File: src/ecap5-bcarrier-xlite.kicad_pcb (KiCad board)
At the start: 2 copper layers, 160 x 60 mm, 48 parts, among them J1 DDR4_SODIMM_Board, J2 DDR4_SODIMM_Board, J3 Conn_02x04_Counter_Clockwise, J5 USB_C_Receptacle_USB2.0_14P, J6 Conn_Coaxial, J7 Conn_Coaxial, J8 Conn_Coaxial, J9 1935161, Q1 BC846BR13, Q2 BC846BR13, SW1 RESET_SOM1, SW2 RESET_SOM2, SW3 USER1, SW4 USER1, U1 FT232RN, U2 AP7375-33SA-7

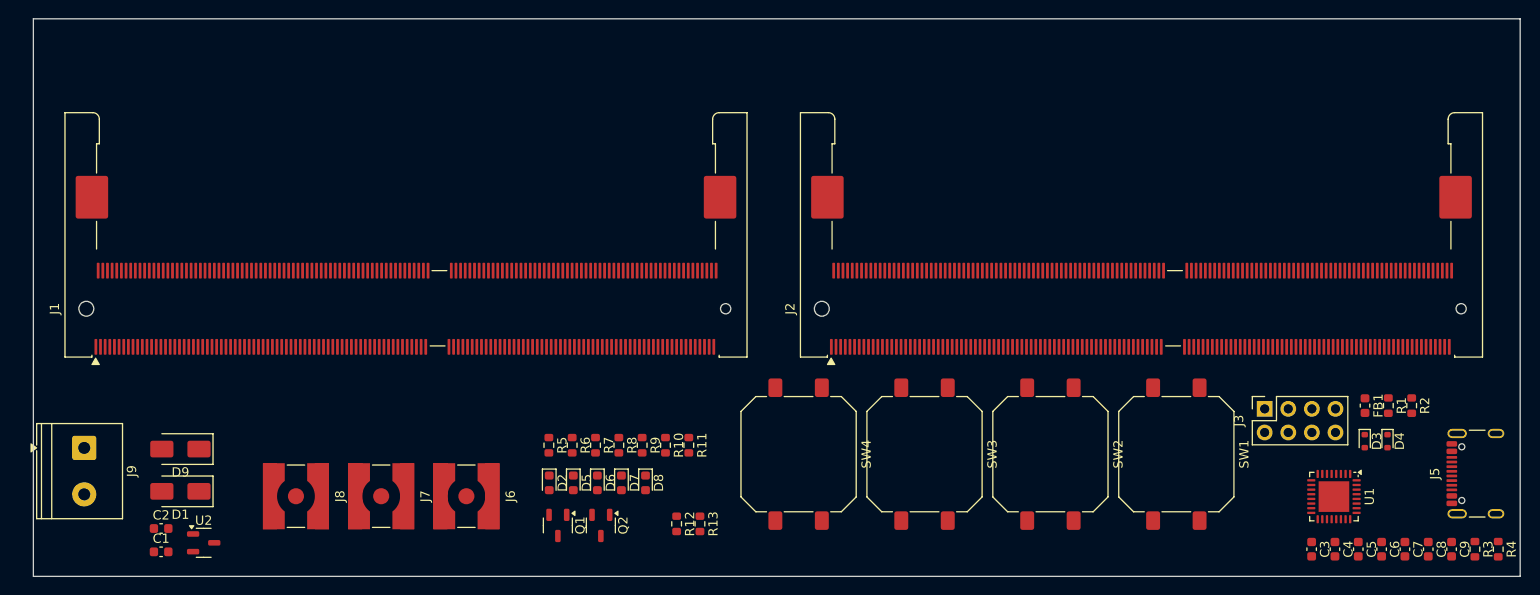
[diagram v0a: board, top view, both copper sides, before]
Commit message: Add power planes
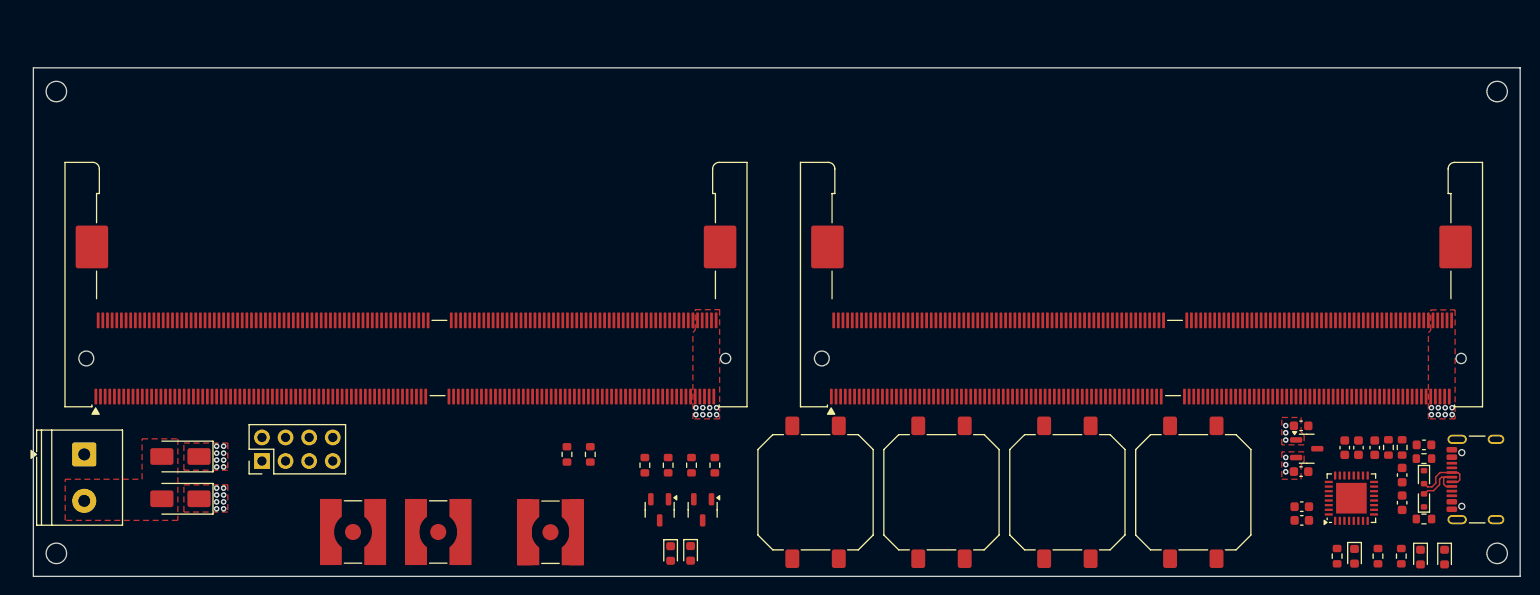
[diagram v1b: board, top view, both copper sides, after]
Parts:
- added H1: MountingHole, MountingHole:MountingHole_2.2mm_M2, F.Cu at (34.7, 66.0)
- added H2: MountingHole, MountingHole:MountingHole_2.2mm_M2, F.Cu at (189.8, 66.0)
- added H3: MountingHole, MountingHole:MountingHole_2.2mm_M2, F.Cu at (189.8, 115.7)
- added H4: MountingHole, MountingHole:MountingHole_2.2mm_M2, F.Cu at (34.7, 115.7)
- J3: footprint Connector_PinSocket_2.54mm:PinSocket_2x04_P2.54mm_Vertical -> Connector_PinHeader_2.54mm:PinHeader_2x04_P2.54mm_Vertical
- moved C1 123.4 mm to (168.7, 102.0)
- moved C2 122.8 mm to (168.7, 106.9)
- moved U2 119.1 mm to (169.3, 104.5)
- moved J3 108.1 mm to (56.9, 105.8)
- moved D6 88.9 mm to (181.5, 116.1)
- moved D7 88.9 mm to (184.1, 116.1)
- moved R7 87.5 mm to (179.5, 116.0)
- moved R6 87.5 mm to (176.9, 116.0)
- moved R5 85.7 mm to (172.6, 116.0)
- moved D5 84.4 mm to (174.4, 116.0)
- moved R4 16.1 mm to (178.1, 104.3), turned to 90 degrees
- moved D2 15.1 mm to (100.8, 115.7)
- moved R12 14.0 mm to (89.7, 105.1)
- moved R13 14.0 mm to (92.2, 105.1)
- moved C9 13.7 mm to (176.6, 104.3), turned to 90 degrees
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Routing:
- net /USB.DP: track 0.00 -> 6.65 mm
- net /USB.DN: track 0.00 -> 6.64 mm
- net VIN9_15: vias 0 -> 27
- net GND: vias 0 -> 8
- net +3V3: vias 0 -> 3
- added copper zone on F.Cu, net +3V3
- added copper zone on In2.Cu, net +3V3
- added copper zone on F.Cu, net GND
- added copper zone on In1.Cu, net GND
- added copper zone on F.Cu, net Net-(D1-A)
- added copper zone on F.Cu, net VIN9_15
- added copper zone on In2.Cu, net VIN9_15
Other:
- board size 160 x 60 mm -> 160 x 54.7 mm
- copper layers 2 -> 4

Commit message: Start routing the usb interface
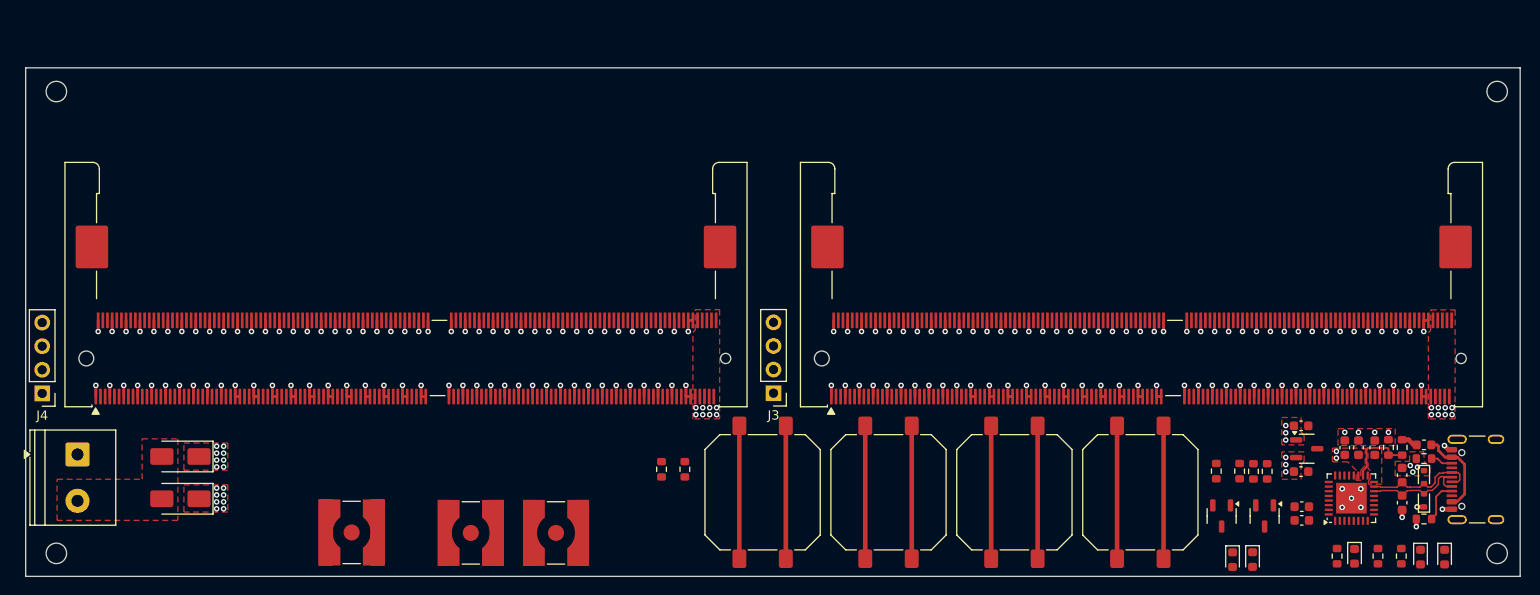
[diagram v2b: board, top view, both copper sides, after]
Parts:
- added J4: Conn_01x04, Connector_PinHeader_2.54mm:PinHeader_1x04_P2.54mm_Vertical, F.Cu at (33.2, 98.5)
- J3: value Conn_02x04_Counter_Clockwise -> Conn_01x04; footprint Connector_PinHeader_2.54mm:PinHeader_2x04_P2.54mm_Vertical -> Connector_PinHeader_2.54mm:PinHeader_1x04_P2.54mm_Vertical
- moved R8 61.5 mm to (159.6, 106.9)
- moved R9 61.5 mm to (162.1, 106.9)
- moved D2 60.5 mm to (161.3, 116.4)
- moved R10 60.5 mm to (163.6, 106.9)
- moved D8 60.5 mm to (163.4, 116.4)
- moved Q1 60.5 mm to (160.1, 111.7)
- moved Q2 60.5 mm to (164.8, 111.7)
- moved R11 59.4 mm to (165.0, 106.9)
- moved J3 55.5 mm to (111.9, 98.5), turned to 180 degrees
- moved J6 21.4 mm to (66.5, 113.5)
- moved J7 12.7 mm to (88.5, 113.5)
- moved J8 12.7 mm to (79.3, 113.5)
- moved R12 10.3 mm to (99.8, 106.7)
- moved R13 10.3 mm to (102.4, 106.7)
- moved R1 6.50 mm to (181.9, 112.0)
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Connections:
- J1 pad 11: /SOM1/JTAG_TDO -> /SOM1.JTAC_TDO
- J1 pad 3: /SOM1/JTAG_TMS -> /SOM1.JTAC_TMS
- J1 pad 5: /SOM1/JTAG_TCK -> /SOM1.JTAC_TCK
- J1 pad 9: /SOM1/JTAG_TDI -> /SOM1.JTAC_TDI
- J2 pad 11: /SOM2/JTAG_TDO -> /SOM2.JTAC_TDO
- J2 pad 3: /SOM2/JTAG_TMS -> /SOM2.JTAC_TMS
- J2 pad 5: /SOM2/JTAG_TCK -> /SOM2.JTAC_TCK
- J2 pad 9: /SOM2/JTAG_TDI -> /SOM2.JTAC_TDI
- J3 pad 1: /SOM1.JTAC_TCK -> /SOM2.JTAC_TCK
- J3 pad 2: /SOM1.JTAC_TDI -> /SOM2.JTAC_TDI
- J3 pad 3: /SOM1.JTAC_TDO -> /SOM2.JTAC_TDO
- J3 pad 4: /SOM1.JTAC_TMS -> /SOM2.JTAC_TMS
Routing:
- net GND: track 0.00 -> 242.8 mm, vias 8 -> 189
- net +3V3: track 0.00 -> 28.6 mm, vias 3 -> 5
- net /SOM2.RESET_IN: track 0.00 -> 14.3 mm
- net /SOM1.RESET_IN: track 0.00 -> 14.3 mm
- net /BUTTON2: track 0.00 -> 14.3 mm
- net /BUTTON1: track 0.00 -> 14.3 mm
- net Net-(FB1-Pad2): track 0.00 -> 9.64 mm
- net Net-(U1-~{RESET}): track 0.00 -> 7.60 mm
- net /USB.DP: track 6.65 -> 12.7 mm
- net /USB.DN: track 6.64 -> 12.6 mm
- net Net-(J5-CC1): track 0.00 -> 4.54 mm
- net Net-(J5-CC2): track 0.00 -> 2.38 mm
- net VBUS: track 0.00 -> 1.79 mm
- added copper zone on F.Cu, net Net-(U1-3V3OUT)
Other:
- board size 160 x 54.7 mm -> 160.8 x 54.7 mm

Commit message: Route more
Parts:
- moved SW1 57.4 mm to (94.0, 109.2), turned to 180 degrees
- moved R13 37.1 mm to (139.2, 102.0), turned to 0 degrees
- moved SW4 34.8 mm to (145.5, 109.2), turned to 180 degrees
- moved SW2 26.7 mm to (111.1, 109.2), turned to 180 degrees
- moved R12 22.7 mm to (122.0, 102.0), turned to 0 degrees
- moved R5 12.0 mm to (184.3, 114.0), turned to 180 degrees
- moved D7 9.38 mm to (174.8, 114.8), turned to 90 degrees
- moved J7 8.43 mm to (80.3, 111.3), turned to 0 degrees
- moved J6 8.43 mm to (58.4, 111.3)
- moved J8 8.43 mm to (71.2, 111.3), turned to 180 degrees
- moved D6 8.30 mm to (173.3, 114.8), turned to 90 degrees
- moved D5 7.79 mm to (182.1, 114.8), turned to 90 degrees
- moved R6 6.18 mm to (171.1, 114.0), turned to 0 degrees
- moved Q2 4.72 mm to (160.2, 110.7)
- moved R9 4.69 mm to (157.4, 106.8), turned to 90 degrees
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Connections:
- J1 pad 147: unconnected-(J1-Pad147) -> /TP.DIFFP
- J1 pad 149: unconnected-(J1-Pad149) -> /TP.DIFFN
- J1 pad 4: /SOM1/RESET_IN -> /SOM1.RESET_IN
- J1 pad 59: unconnected-(J1-Pad59) -> /TP.SINGLEENDED
- J2 pad 4: /SOM2/RESET_IN -> /SOM2.RESET_IN
- Q1 pad 1: (no net) -> Net-(Q1-B)
- Q1 pad 2: (no net) -> GND
- Q1 pad 3: (no net) -> Net-(D2-K)
- Q2 pad 1: (no net) -> Net-(Q2-B)
- Q2 pad 2: (no net) -> GND
- Q2 pad 3: (no net) -> Net-(D8-K)
- R11 pad 1: Net-(Q2-PadB) -> Net-(Q2-B)
- R9 pad 1: Net-(Q1-PadB) -> Net-(Q1-B)
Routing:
- net GND: track 242.8 -> 316.1 mm, vias 189 -> 221
- net /SOM1.RESET_IN: track 14.3 -> 74.9 mm, vias 0 -> 2
- net /SOM2.JTAC_TMS: track 0.00 -> 18.5 mm
- net /SOM1.JTAC_TMS: track 0.00 -> 17.9 mm
- net /TP.DIFFP: track 0.00 -> 17.0 mm
- net /TP.DIFFN: track 0.00 -> 17.0 mm
- net /SOM2.RESET_IN: track 14.3 -> 30.7 mm, vias 0 -> 2
- net /TP.SINGLEENDED: track 0.00 -> 14.5 mm
- net /SOM2.JTAC_TDO: track 0.00 -> 11.9 mm
- net /SOM1.JTAC_TDO: track 0.00 -> 11.9 mm
- net /SOM1.JTAC_TDI: track 0.00 -> 9.97 mm
- net /SOM2.JTAC_TDI: track 0.00 -> 9.97 mm
- net +3V3: track 28.6 -> 37.6 mm, vias 5 -> 16
- net /SOM2.JTAC_TCK: track 0.00 -> 8.76 mm
- net /SOM1.JTAC_TCK: track 0.00 -> 8.76 mm
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
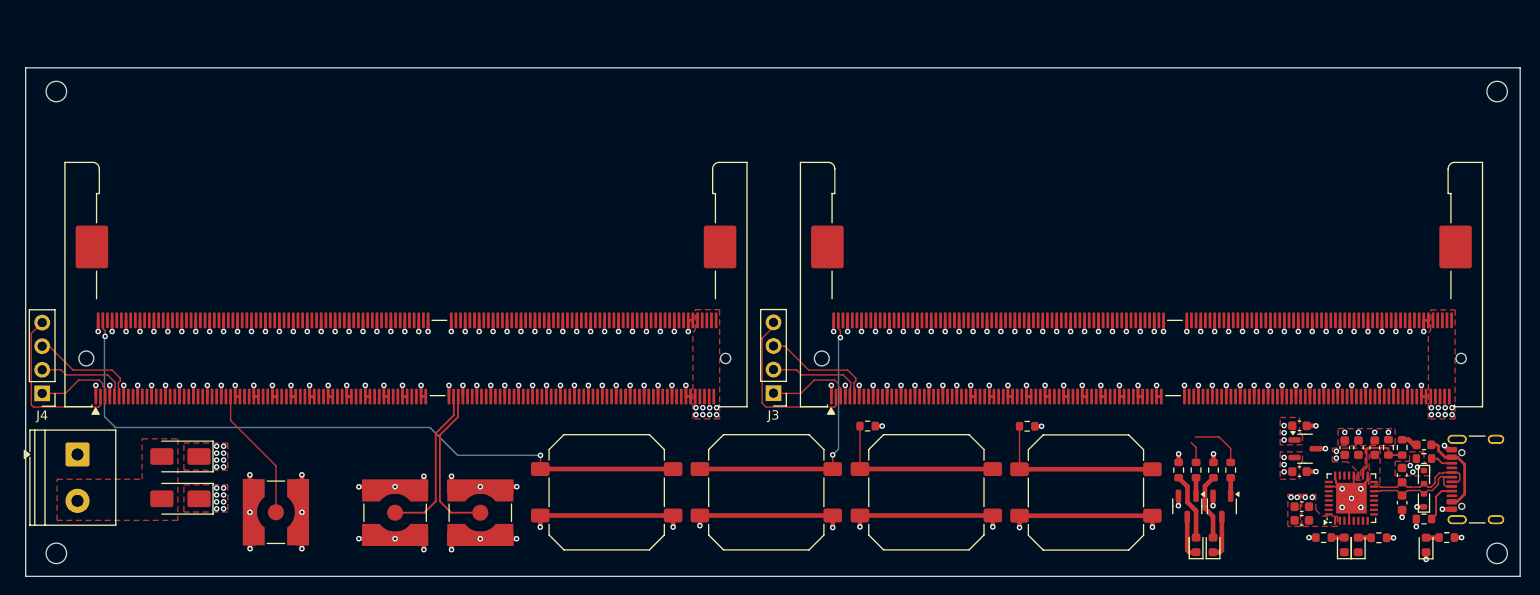
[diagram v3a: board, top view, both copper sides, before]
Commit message: Route the LVDS pairs
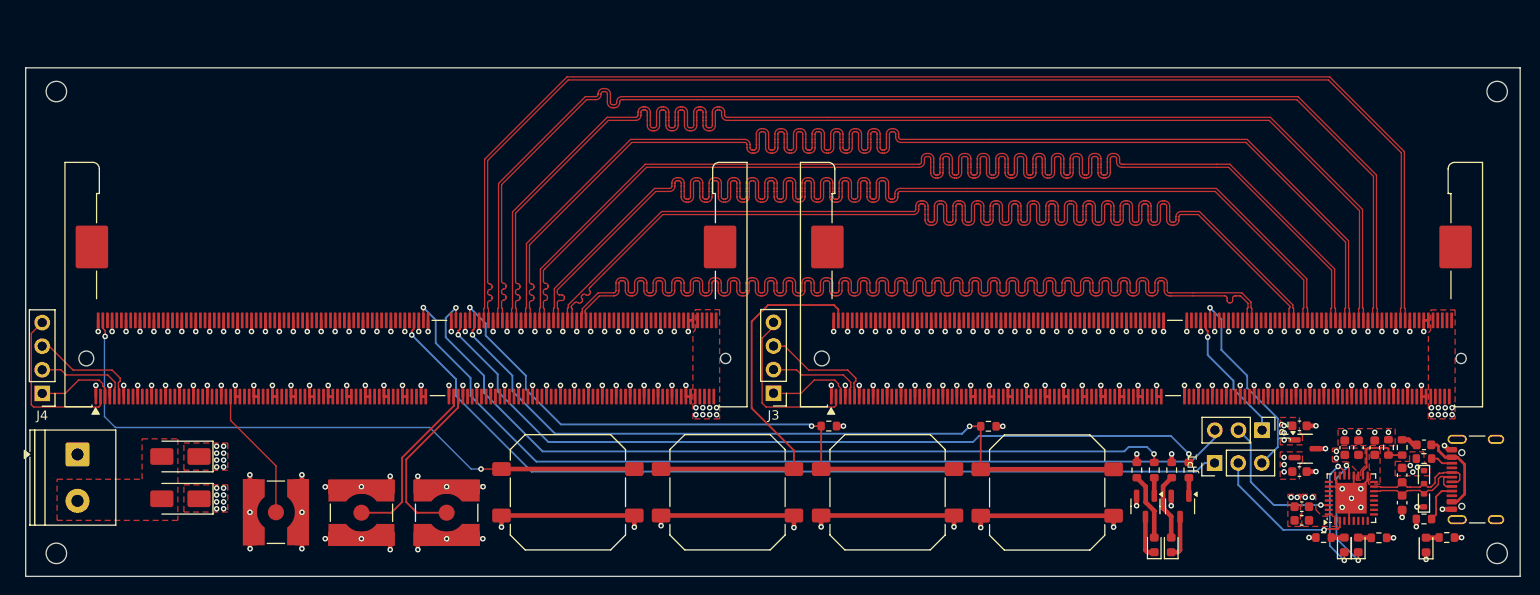
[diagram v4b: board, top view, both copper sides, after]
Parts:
- added JP1: Jumper_3_Open, Connector_PinHeader_2.54mm:PinHeader_1x03_P2.54mm_Vertical, F.Cu at (159.4, 106.0)
- added JP2: Jumper_3_Open, Connector_PinHeader_2.54mm:PinHeader_1x03_P2.54mm_Vertical, F.Cu at (164.5, 102.5)
- moved D2 4.50 mm to (152.9, 114.8)
- moved D8 4.50 mm to (154.7, 114.8)
- moved Q1 4.50 mm to (151.9, 110.7)
- moved Q2 4.50 mm to (155.7, 110.7)
- moved R10 4.50 mm to (154.8, 106.8)
- moved R11 4.50 mm to (156.6, 106.8)
- moved R8 4.50 mm to (151.0, 106.8)
- moved R9 4.50 mm to (152.9, 106.8)
- moved R12 4.18 mm to (117.8, 102.0)
- moved SW4 4.18 mm to (141.3, 109.2)
- moved SW1 4.17 mm to (89.8, 109.2)
- moved SW2 4.17 mm to (107.0, 109.2)
- moved SW3 4.17 mm to (124.2, 109.2)
- moved R13 4.17 mm to (135.0, 102.0)
- moved J7 3.62 mm to (76.7, 111.3)
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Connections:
- J1 pad 138: unconnected-(J1-Pad138) -> /SOM1.UART_RX
- J1 pad 142: unconnected-(J1-Pad142) -> /SOM1.UART_TX
- J1 pad 148: unconnected-(J1-Pad148) -> /LED1
- J1 pad 150: unconnected-(J1-Pad150) -> /LED2
- J1 pad 154: unconnected-(J1-Pad154) -> /BUTTON1
- J1 pad 156: unconnected-(J1-Pad156) -> /BUTTON2
- J1 pad 160: unconnected-(J1-Pad160) -> /SOM1/RTD17P
- J1 pad 162: unconnected-(J1-Pad162) -> /SOM1/RTD17N
- J1 pad 166: unconnected-(J1-Pad166) -> /SOM1/RTD18P
- J1 pad 168: unconnected-(J1-Pad168) -> /SOM1/RTD18N
- J1 pad 172: unconnected-(J1-Pad172) -> /SOM1/RTD19P
- J1 pad 174: unconnected-(J1-Pad174) -> /SOM1/RTD19N
- J1 pad 178: unconnected-(J1-Pad178) -> /SOM1/RTD20N
- J1 pad 180: unconnected-(J1-Pad180) -> /SOM1/RTD20P
- J1 pad 184: unconnected-(J1-Pad184) -> /SOM1/RTD21N
- J1 pad 186: unconnected-(J1-Pad186) -> /SOM1/RTD21P
- J1 pad 190: unconnected-(J1-Pad190) -> /SOM1/RTD22N
- J1 pad 192: unconnected-(J1-Pad192) -> /SOM1/RTD22P
- J1 pad 196: unconnected-(J1-Pad196) -> /SOM1/RTD23P
- J1 pad 198: unconnected-(J1-Pad198) -> /SOM1/RTD23N
- J1 pad 202: unconnected-(J1-Pad202) -> /SOM1/RTD24N
- J1 pad 204: unconnected-(J1-Pad204) -> /SOM1/RTD24P
- J2 pad 154: unconnected-(J2-Pad154) -> /SOM2.UART_TX
- J2 pad 156: unconnected-(J2-Pad156) -> /SOM2.UART_RX
- J2 pad 172: unconnected-(J2-Pad172) -> /SOM1/RTD24P
- J2 pad 174: unconnected-(J2-Pad174) -> /SOM1/RTD24N
- J2 pad 190: unconnected-(J2-Pad190) -> /SOM1/RTD23N
- J2 pad 192: unconnected-(J2-Pad192) -> /SOM1/RTD23P
- J2 pad 196: unconnected-(J2-Pad196) -> /SOM1/RTD22P
- J2 pad 198: unconnected-(J2-Pad198) -> /SOM1/RTD22N
- J2 pad 208: unconnected-(J2-Pad208) -> /SOM1/RTD21P
- J2 pad 210: unconnected-(J2-Pad210) -> /SOM1/RTD21N
- J2 pad 214: unconnected-(J2-Pad214) -> /SOM1/RTD20P
- J2 pad 216: unconnected-(J2-Pad216) -> /SOM1/RTD20N
- J2 pad 220: unconnected-(J2-Pad220) -> /SOM1/RTD19N
- J2 pad 222: unconnected-(J2-Pad222) -> /SOM1/RTD19P
- J2 pad 226: unconnected-(J2-Pad226) -> /SOM1/RTD18N
- J2 pad 228: unconnected-(J2-Pad228) -> /SOM1/RTD18P
- J2 pad 238: unconnected-(J2-Pad238) -> /SOM1/RTD17N
- J2 pad 240: unconnected-(J2-Pad240) -> /SOM1/RTD17P
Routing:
- net /SOM1/RTD24N: track 0.00 -> 151.3 mm
- net /SOM1/RTD24P: track 0.00 -> 151.3 mm
- net /SOM1/RTD21N: track 0.00 -> 146.2 mm
- net /SOM1/RTD21P: track 0.00 -> 146.2 mm
- net /SOM1/RTD20N: track 0.00 -> 144.9 mm
- net /SOM1/RTD20P: track 0.00 -> 144.8 mm
- net /SOM1/RTD22N: track 0.00 -> 143.2 mm
- net /SOM1/RTD22P: track 0.00 -> 143.2 mm
- net /SOM1/RTD23P: track 0.00 -> 143.1 mm
- net /SOM1/RTD23N: track 0.00 -> 143.0 mm
- net /SOM1/RTD17P: track 0.00 -> 141.5 mm
- net /SOM1/RTD17N: track 0.00 -> 141.5 mm
- net /SOM1/RTD19P: track 0.00 -> 139.9 mm
- net /SOM1/RTD19N: track 0.00 -> 139.8 mm
- net /SOM1/RTD18P: track 0.00 -> 134.6 mm
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- added copper zone on In2.Cu, net GND
